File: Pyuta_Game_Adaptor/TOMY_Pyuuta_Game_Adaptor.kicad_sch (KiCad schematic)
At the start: 7 parts, among them J1 Tomy Pyūta I/O Port, J2 Tomy Pyūta Cartridge

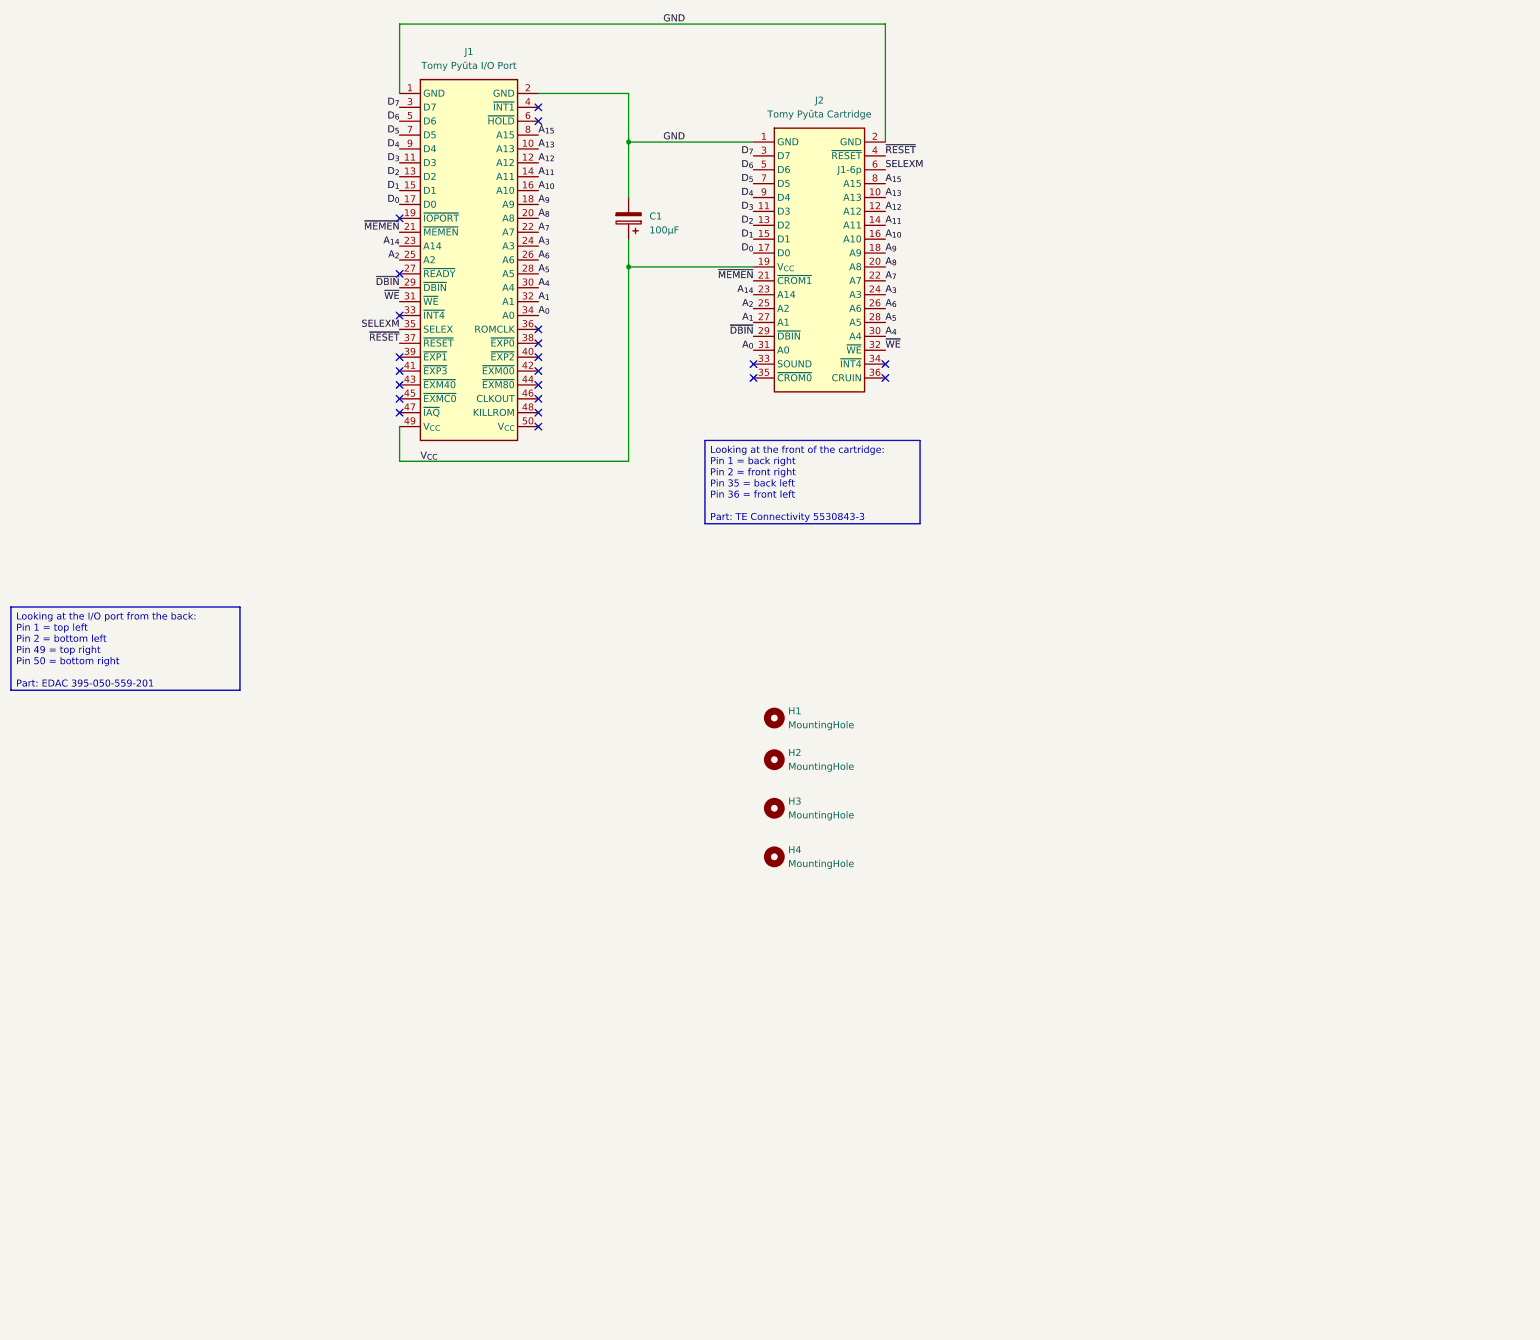
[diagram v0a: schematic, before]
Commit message: Added info about unused parts to schematic
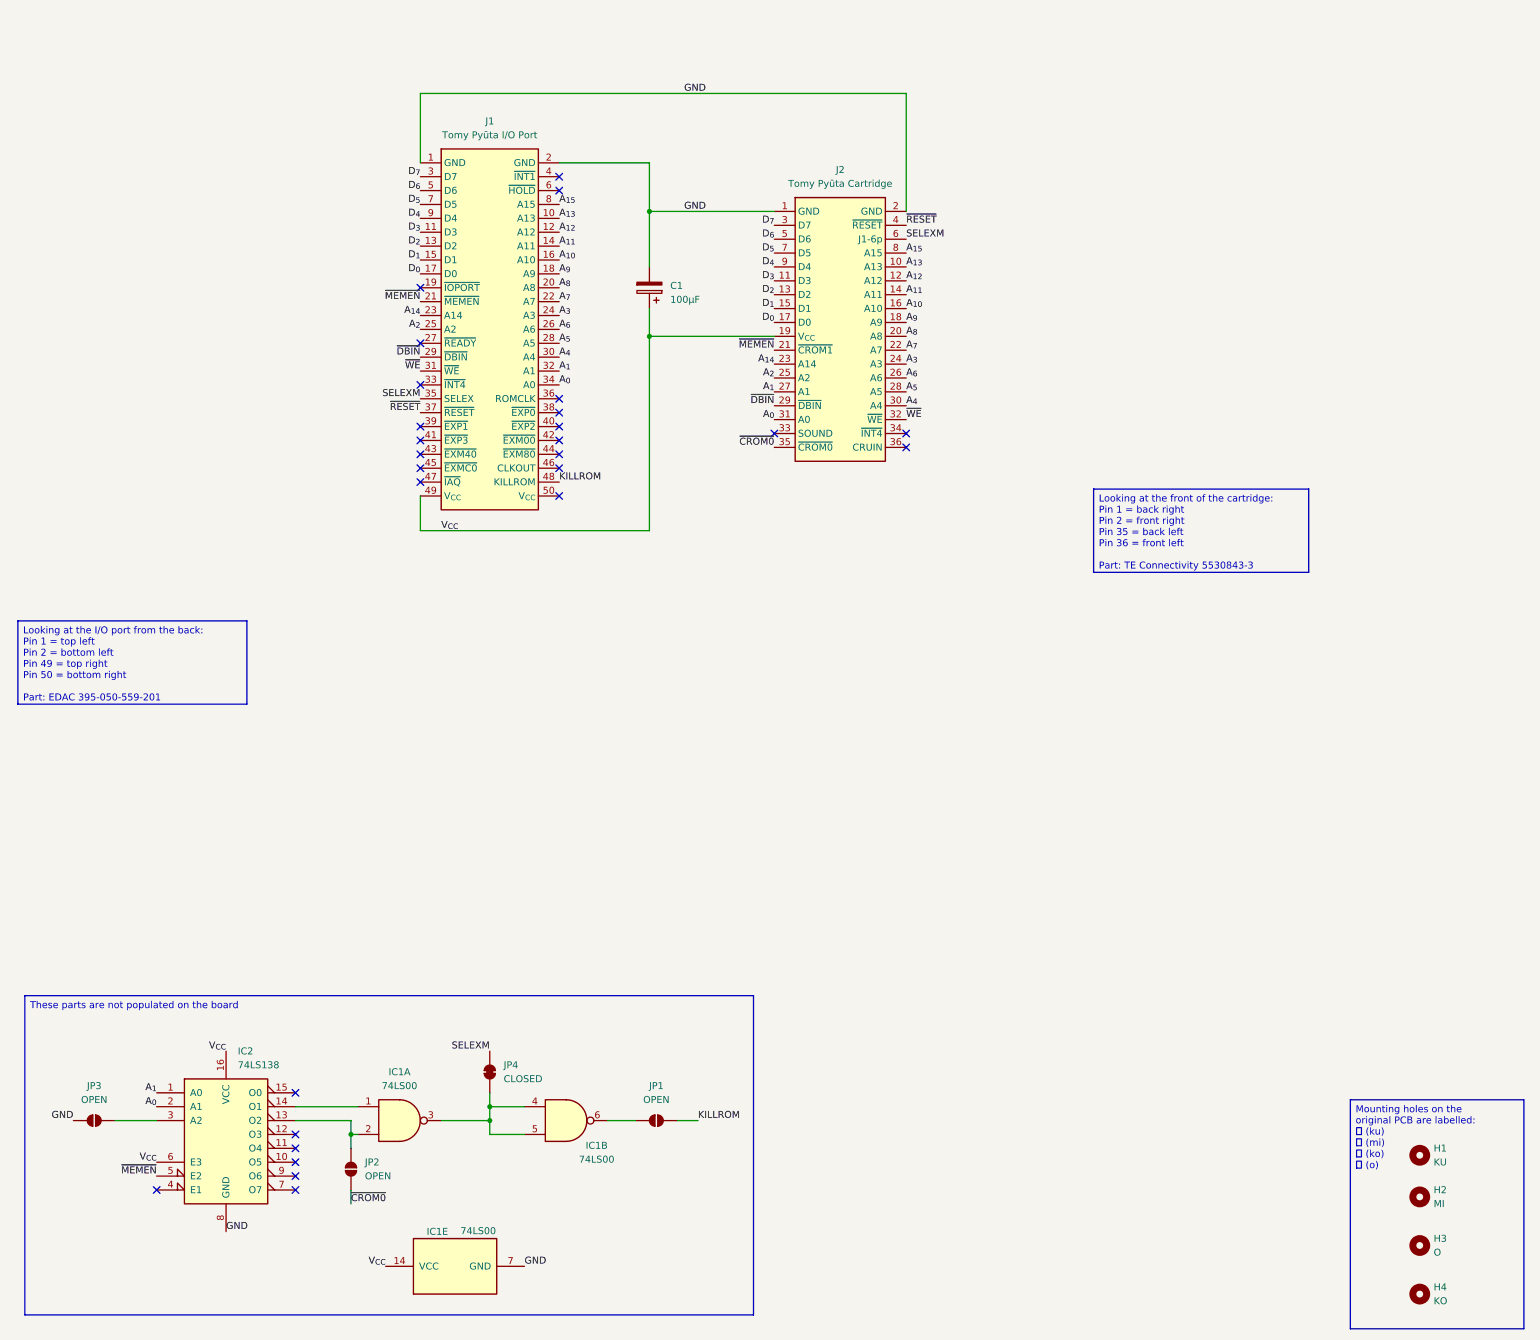
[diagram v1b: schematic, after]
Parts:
- added IC1: 74LS00, symbol 74xx:74LS00
- added IC2: 74LS138, symbol 74xx:74LS138
- added JP1, JP2, JP3: OPEN, symbol Jumper:SolderJumper_2_Open
- added JP4: CLOSED, symbol Jumper:SolderJumper_2_Bridged
- H1: value MountingHole -> KU
- H2: value MountingHole -> MI
- H3: value MountingHole -> O
- H4: value MountingHole -> KO
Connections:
- net A_{0}: now also IC2.2 (A1)
- net A_{1}: now also IC2.1 (A0)
- net GND: now also IC1.7 (GND), IC2.8 (GND), JP3.2 (B)
- net SELEXM: now also JP4.2 (B)
- net V_{CC}: now also IC1.14 (VCC), IC2.16 (VCC), IC2.6 (E3)
- net ~{MEMEN}: now also IC2.5 (E2)
- net KILLROM: now reaches J1.48 (KILLROM)
- net KILLROM: now also JP1.2 (B)
- net ~{CROM0}: now reaches J2.35 (~{CROM0})
- net ~{CROM0}: now also JP2.1 (A)
- new net: IC1.6, JP1.1 (A)
- new net: IC1.2, IC2.13 (O2), JP2.2 (B)
- new net: IC1.1, IC2.14 (O1)
- new net: IC1.3, IC1.4, IC1.5, JP4.1 (A)
- new net: IC2.3 (A2), JP3.1 (A)
- no-connect marks 22 -> 27
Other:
- moved on the sheet: C1, H1, H2, H3, H4, J1, J2
